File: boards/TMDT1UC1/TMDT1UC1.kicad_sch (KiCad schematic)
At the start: 26 parts, among them U1 DW3210, U2 STM32U575RGTx, U3 LIS2DH, U4 TPS61222DCK

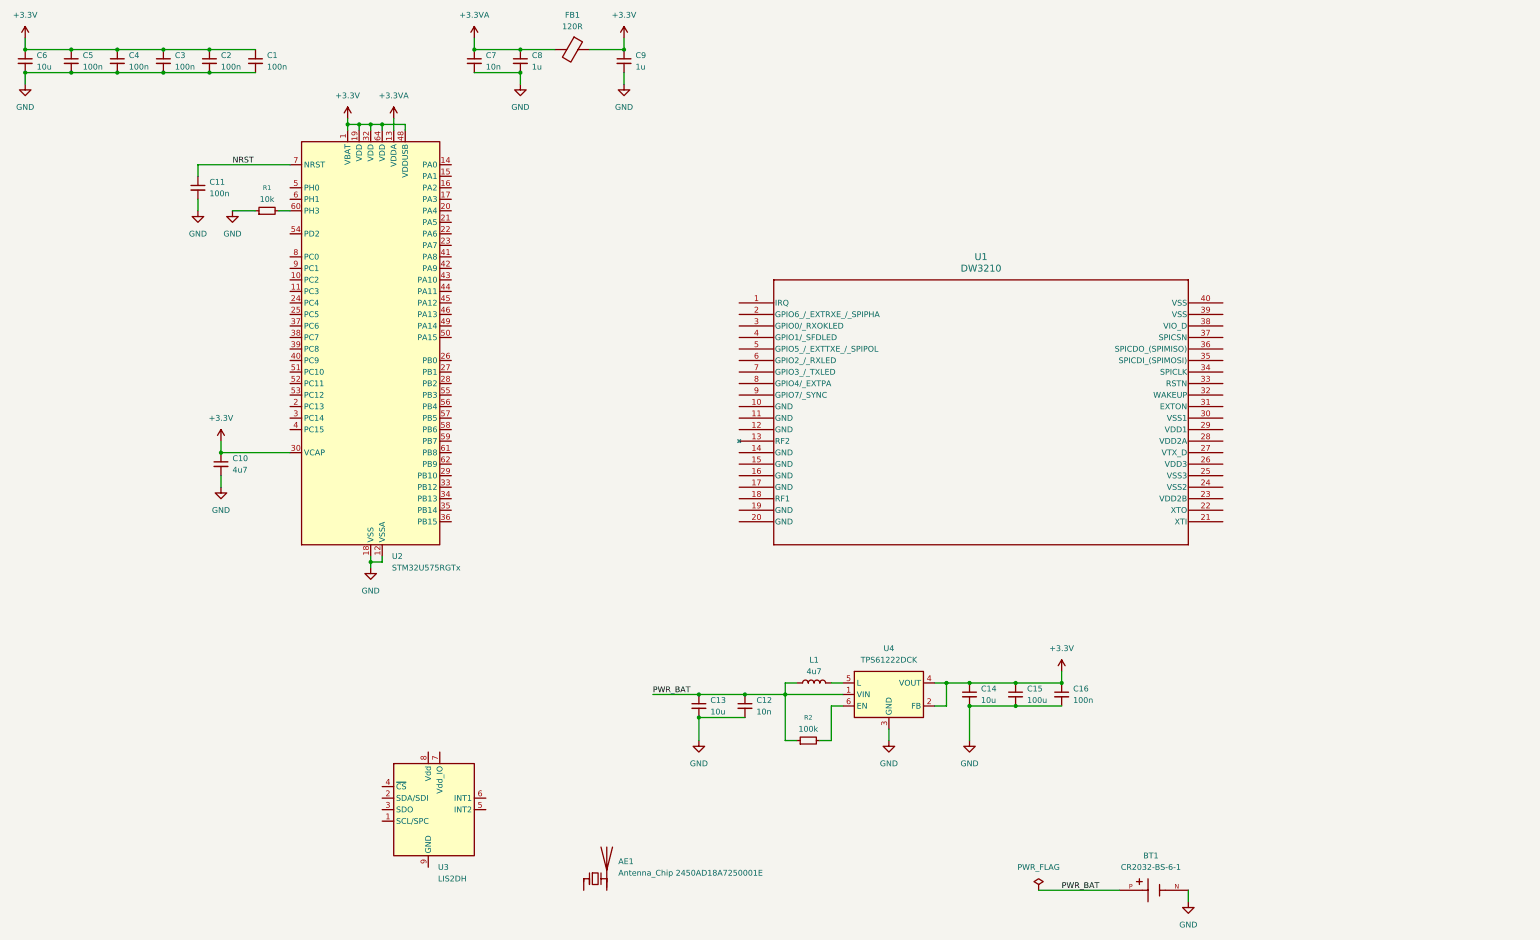
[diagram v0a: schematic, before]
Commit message: Added initial power and RF. (no SPI comms) for tag STM2DW
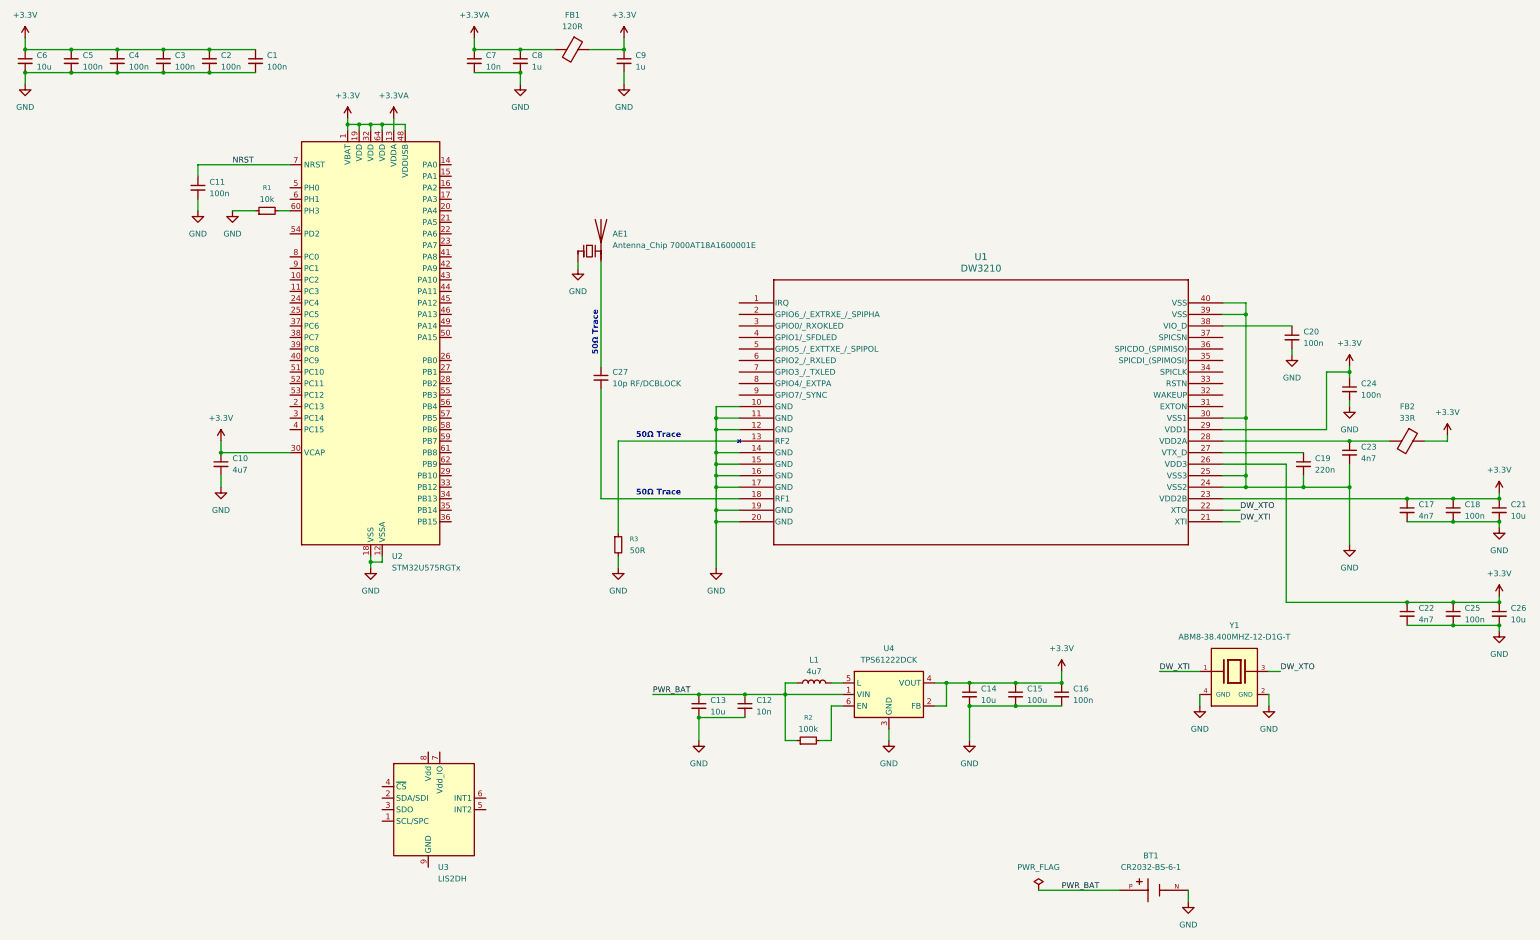
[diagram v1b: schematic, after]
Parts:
- added C17, C22, C23: 4n7, symbol Device:C_Small
- added C18, C20, C24, C25: 100n, symbol Device:C_Small
- added C19: 220n, symbol Device:C_Small
- added C21, C26: 10u, symbol Device:C_Small
- added C27: 10p RF/DCBLOCK, symbol Device:C_Small
- added FB2: 33R, symbol Device:FerriteBead
- added R3: 50R, symbol Device:R_Small
- added Y1: ABM8-38.400MHZ-12-D1G-T, meridian:XTAL_ABM8-38.400MHZ-12-D1G-T, symbol ABM8-38.400MHZ-12-D1G-T:ABM8-38.400MHZ-12-D1G-T
- AE1: value Antenna_Chip 2450AD18A7250001E -> Antenna_Chip 7000AT18A1600001E
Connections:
- net +3.3V: now also U1.23 (VDD2B), U1.26 (VDD3), U1.29 (VDD1), C17.1, C18.1, C21.1, C22.1, C24.1, C25.1, C26.1, FB2.1
- net GND: now also AE1.1 (FEED), U1.10 (GND), U1.11 (GND), U1.12 (GND), U1.14 (GND), U1.15 (GND), U1.16 (GND), U1.17 (GND), U1.19 (GND), U1.20 (GND), U1.24 (VSS2), U1.25 (VSS3), U1.30 (VSS1), U1.39 (VSS), U1.40 (VSS), C17.2, C18.2, C19.2, C20.2, C21.2, C22.2, C23.2, C24.2, C25.2, C26.2, R3.2, Y1.2 (GND), Y1.4 (GND)
- net at AE1.2 (PCB_Trace): now also C27.1
- net at U1.13 (RF2): now also R3.1
- net at U1.18 (RF1): now also C27.2
- net DW_XTI: now reaches U1.21 (XTI)
- net DW_XTI: now also Y1.1
- net DW_XTO: now reaches U1.22 (XTO)
- net DW_XTO: now also Y1.3
- net at U1.27 (VTX_D): now also C19.1
- net at U1.28 (VDD2A): now also C23.1, FB2.2
- net at U1.38 (VIO_D): now also C20.1
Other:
- note added: "50Ω Trace"
- moved on the sheet: AE1
